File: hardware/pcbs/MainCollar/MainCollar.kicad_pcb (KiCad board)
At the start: 2 copper layers, 79 parts, among them J1 SMA-EDGE, M1 Mounting_Hole, M2 Mounting_Hole, M3 Mounting_Hole, M4 Mounting_Hole, P1 USB_OTG, P2 CONN_01X05, P3 Solar1, P4 Solar2, P5 CONN_02X05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

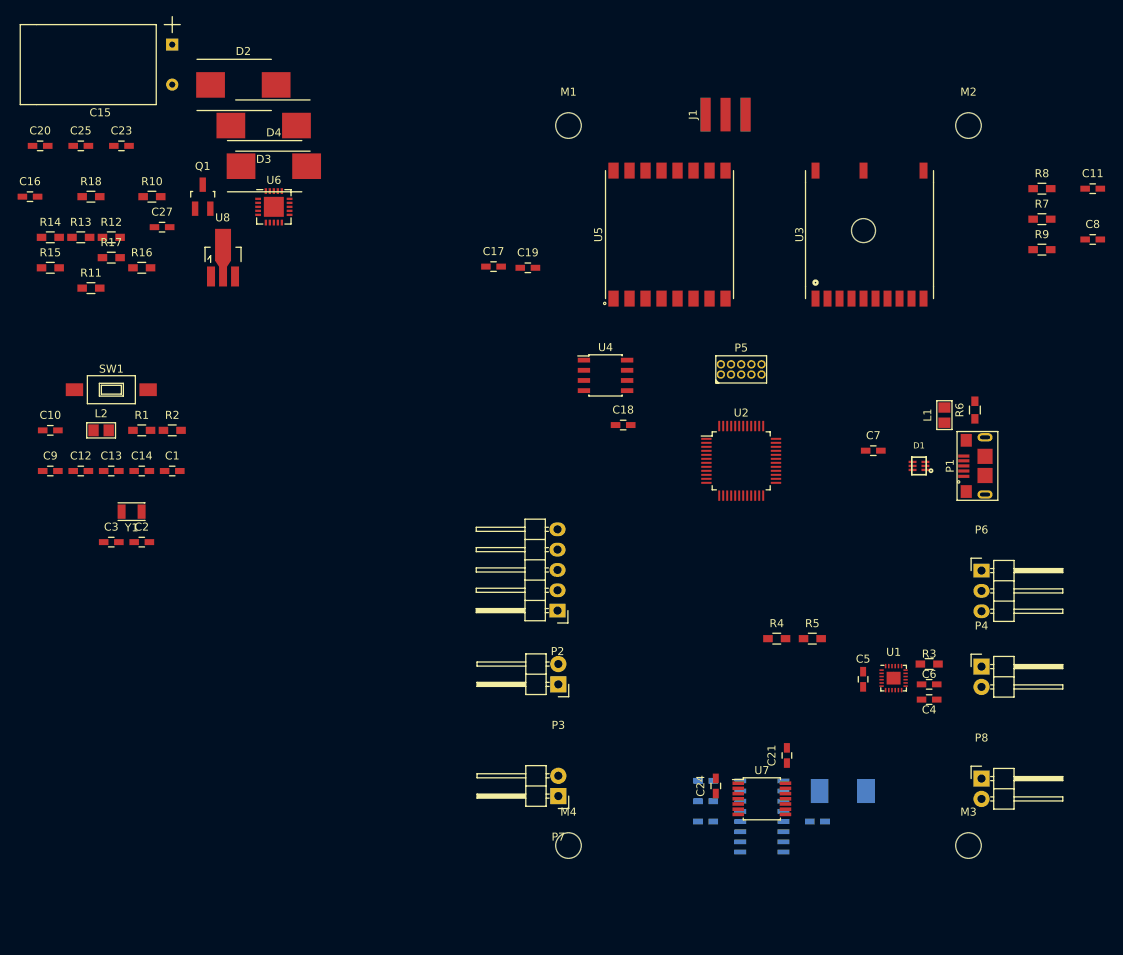
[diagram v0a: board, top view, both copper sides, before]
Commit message: Initial PCB component placement
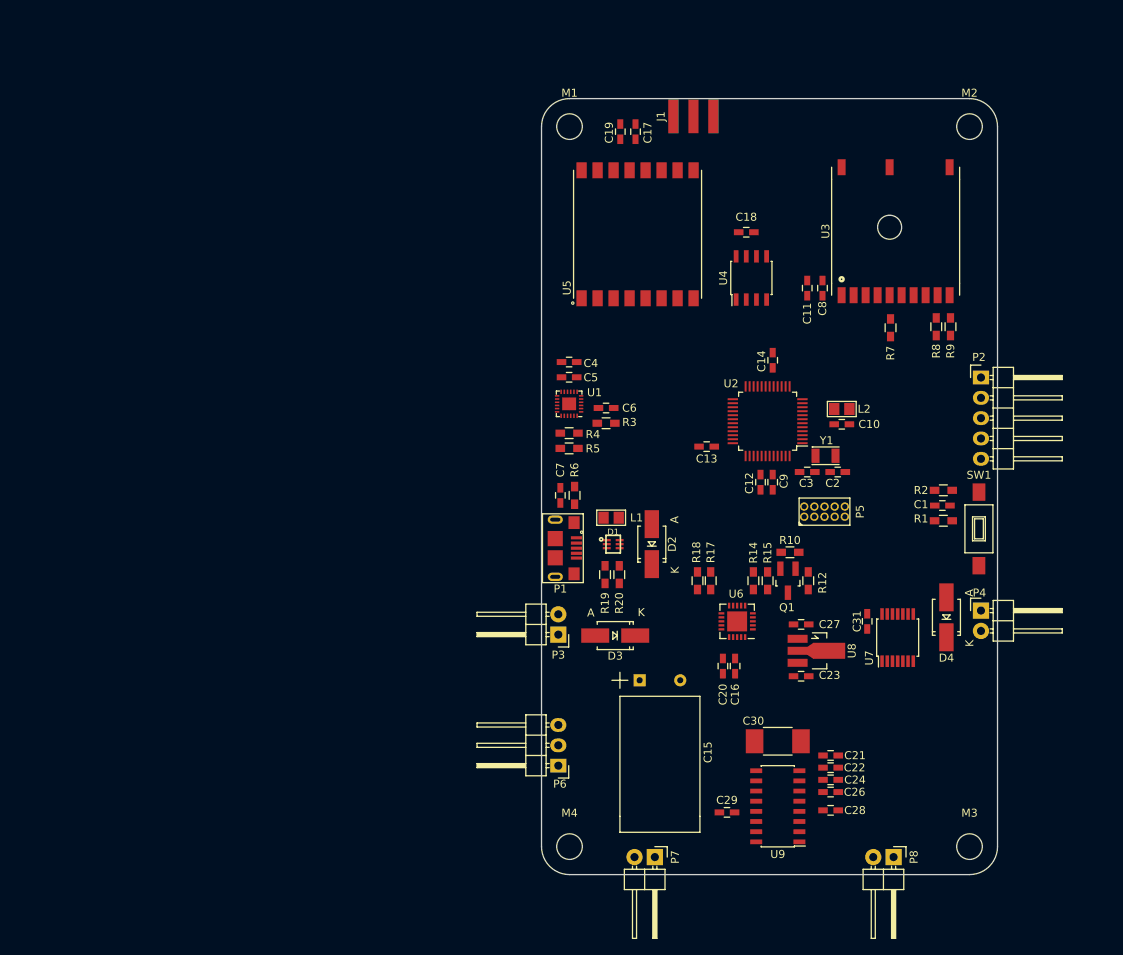
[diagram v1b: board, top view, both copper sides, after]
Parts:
- removed C25: 1uF, Capacitors_SMD:C_0603_HandSoldering
- removed R11, R13, R16: 10K, Resistors_SMD:R_0603_HandSoldering
- added C31: 0.1uF, Capacitors_SMD:C_0603_HandSoldering, F.Cu at (76.7, 101.3)
- added R19: 100K, Resistors_SMD:R_0603_HandSoldering, F.Cu at (43.9, 95.5)
- added R20: 330, Resistors_SMD:R_0603_HandSoldering, F.Cu at (45.7, 95.5)
- C15: footprint OpenFence:Cap1017 -> Cap1017
- C22, C26, C28, C29, C30, U9: moved to F.Cu
- D2, D3, D4: footprint Diodes_SMD:DO-214AB_Handsoldering -> Diodes_SMD:SMA_Handsoldering
- moved SW1 109.8 mm to (90.7, 89.8), turned to 90 degrees
- moved C23 107.8 mm to (68.5, 108.2)
- moved C20 107.3 mm to (58.7, 106.9), turned to 270 degrees
- moved C16 105.9 mm to (60.2, 106.9), turned to 270 degrees
- moved D4 101.2 mm to (86.6, 100.8), turned to 90 degrees
- moved R1 100.8 mm to (86.2, 88.8), turned to 180 degrees
- moved C10 98.9 mm to (73.5, 76.7)
- moved C15 98.2 mm to (50.8, 108.7), turned to 90 degrees
- moved R15 97.8 mm to (64.3, 96.3), turned to 90 degrees
- moved R14 97.8 mm to (62.5, 96.3), turned to 270 degrees
- moved R12 97.1 mm to (69.3, 96.3), turned to 270 degrees
- moved R2 96.7 mm to (86.2, 85.0)
- moved C1 96.4 mm to (86.1, 86.9)
- moved C27 94.1 mm to (68.5, 101.7), turned to 180 degrees
- moved L2 92.6 mm to (73.5, 74.8)
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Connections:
- P2 pad 2: /AUX_1 -> /AUX_3
- P2 pad 4: /AUX_3 -> /AUX_1
- P3 pad 1: GND -> Net-(D3-Pad2)
- P3 pad 2: Net-(D3-Pad2) -> GND
- P4 pad 1: GND -> Net-(D4-Pad2)
- P4 pad 2: Net-(D4-Pad2) -> GND
- U2 pad 13: /Flash_CS -> Net-(U2-Pad13)
- U2 pad 15: Net-(U2-Pad15) -> /GPS_RXD
- U2 pad 16: Net-(U2-Pad16) -> /GPS_TXD
- U2 pad 22: Net-(U2-Pad22) -> /Flash_CS
- U2 pad 28: /~PG -> Net-(U2-Pad28)
- U2 pad 29: /STAT2 -> Net-(U2-Pad29)
- U2 pad 30: /STAT1 -> Net-(U2-Pad30)
- U2 pad 37: /GPS_RXD -> Net-(U2-Pad37)
- U2 pad 38: /GPS_TXD -> Net-(U2-Pad38)
- U2 pad 39: Net-(U2-Pad39) -> /STAT1
- U2 pad 47: Net-(U2-Pad47) -> /STAT2
- U2 pad 48: Net-(U2-Pad48) -> /~PG
- U9 pad 1: Net-(P7-Pad1) -> Net-(P8-Pad2)
- U9 pad 14: Net-(P8-Pad1) -> Net-(P7-Pad2)
- U9 pad 16: Net-(P8-Pad2) -> Net-(P7-Pad1)
- U9 pad 3: Net-(P7-Pad2) -> Net-(P8-Pad1)
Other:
- board outline added: 57 x 97 mm
- net class Power added: clearance 0.0254, trace_width 0.508, via_dia 0.635, via_drill 0.381

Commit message: PCB Prototype Completed
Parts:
- C15: footprint Cap1017 -> OpenFence:Cap1017
- P2: footprint Pin_Headers:Pin_Header_Angled_1x05 -> Pin_Headers:Pin_Header_Straight_1x05
- P3, P4, P7, P8: footprint Pin_Headers:Pin_Header_Angled_1x02 -> Pin_Headers:Pin_Header_Straight_1x02
- P6: footprint Pin_Headers:Pin_Header_Angled_1x03 -> Pin_Headers:Pin_Header_Straight_1x03
- U1: footprint Housings_DFN_QFN:QFN-24-1EP_3x3mm_Pitch0.4mm -> OpenFence:MPU9250
- moved C19 18.9 mm to (62.0, 50.0)
- moved C17 15.9 mm to (60.2, 50.0)
- moved R5 12.0 mm to (51.3, 78.0), turned to 90 degrees
- moved R4 10.1 mm to (49.5, 76.7), turned to 90 degrees
- moved U7 7.64 mm to (80.0, 111.0)
- moved P5 7.37 mm to (71.6, 95.0), turned to 270 degrees
- moved C31 7.00 mm to (75.3, 108.2), turned to 0 degrees
- moved R12 5.22 mm to (65.4, 99.7), turned to 0 degrees
- moved R3 4.78 mm to (39.4, 77.5), turned to 0 degrees
- moved C5 4.62 mm to (44.1, 71.0), turned to 0 degrees
- moved P6 4.06 mm to (38.1, 115.3)
- moved C18 3.43 mm to (63.8, 50.0), turned to 90 degrees
- moved C21 3.05 mm to (72.1, 121.2)
- moved C24 3.05 mm to (72.1, 118.1)
- moved C13 2.64 mm to (58.2, 81.7), turned to 270 degrees
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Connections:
- L1 pad 1: Net-(L1-Pad1) -> VUSB
- P1 pad 1: Net-(L1-Pad1) -> VUSB
- R19 pad 2: +3V3 -> VUSB
- U2 pad 14: Net-(U2-Pad14) -> /GPS_FIX
- U2 pad 26: /GPS_FIX -> Net-(U2-Pad26)
- U2 pad 27: /AMP_SD -> Net-(U2-Pad27)
- U2 pad 8: Net-(U2-Pad8) -> /AMP_SD
- U3 pad 4: VBAT -> +3V3
- U9 pad 10: Net-(C21-Pad1) -> Net-(C24-Pad1)
- U9 pad 7: Net-(C24-Pad1) -> Net-(C21-Pad1)
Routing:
- net GND: track 0.00 -> 527.4 mm, vias 0 -> 150
- net +3V3: track 0.00 -> 217.2 mm, vias 0 -> 17
- net VCC: track 0.00 -> 87.1 mm, vias 0 -> 4
- net /AMP_SD: track 0.00 -> 78.0 mm, vias 0 -> 2
- net /SCL: track 0.00 -> 62.5 mm, vias 0 -> 2
- net /SDA: track 0.00 -> 62.3 mm, vias 0 -> 2
- net /~RESET~: track 0.00 -> 52.3 mm, vias 0 -> 2
- net /AudioIn: track 0.00 -> 49.6 mm, vias 0 -> 2
- net /MOSI: track 0.00 -> 38.4 mm, vias 0 -> 2
- net /RF_INT: track 0.00 -> 36.7 mm, vias 0 -> 2
- net Net-(P6-Pad2): track 0.00 -> 35.6 mm, vias 0 -> 1
- net /MISO: track 0.00 -> 35.2 mm
- net /SCK: track 0.00 -> 34.2 mm
- net VBAT: track 0.00 -> 33.0 mm, vias 0 -> 3
- net VOUT: track 0.00 -> 32.7 mm, vias 0 -> 3
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- added copper zone on B.Cu, net +3V3
- added copper zone on F.Cu, net +3V3
- added copper zone on B.Cu, net GND
- added copper zone on F.Cu, net GND
- added copper zone on F.Cu, net VBAT
- added copper zone on F.Cu, net VCC
- added copper zone on F.Cu, net VOUT
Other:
- rule trace_min: 0.1524 -> 0.006
- rule via_min_size: 0.635 -> 0.025
- board text added: "05-2016"
- board text added: "OpenFence Collar v0.1 Engineer: Alex Muir"
